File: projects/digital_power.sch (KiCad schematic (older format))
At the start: 5 parts, among them U501 LT1763

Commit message: updated LED indicators in schematic files (*.sch)
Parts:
- removed D?: LED_G, symbol LED
- added D?: GREEN_LED, symbol GREEN_LED
- added R?: 121, symbol R
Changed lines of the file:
@@
 LIBS:microchip_gosselin
 LIBS:linear_technology_gosselin
+LIBS:led_gosselin
 LIBS:mStereo2-cache
 EELAYER 24 0
@@
 	4450 4650 7000 4650
 $Comp
-L LED D?
-U 1 1 544F5650
-P 8100 4100
-F 0 "D?" H 8100 4200 50  0000 C CNN
-F 1 "LED_G" H 8100 4000 50  0000 C CNN
-F 2 "" H 8100 4100 60  0000 C CNN
-F 3 "" H 8100 4100 60  0000 C CNN
-	1    8100 4100
+L GREEN_LED D?
+U 1 1 5454AC46
+P 4000 4300
+F 0 "D?" H 4000 4400 50  0000 C CNN
+F 1 "GREEN_LED" H 4000 4200 50  0000 C CNN
+F 2 "" H 4000 4300 60  0000 C CNN
+F 3 "" H 4000 4300 60  0000 C CNN
+F 4 " 160-1423-1-ND" H 4200 4600 60  0001 C CNN "Supplier-PN"
+F 5 "Digi-key" H 4100 4500 60  0001 C CNN "Supplier"
+F 6 "LED GREEN CLEAR THIN 0805 SMD" H 4500 4900 60  0001 C CNN "Description"
+F 7 "Lite-On" H 4300 4700 60  0001 C CNN "Manu"
+F 8 "LTST-C171GKT" H 4400 4800 60  0001 C CNN "Manu-PN"
+	1    4000 4300
 	0    1    1    0
 $EndComp
+$Comp
+L R R?
+U 1 1 5454CACE
+P 3700 4300
+F 0 "R?" V 3780 4300 40  0000 C CNN
+F 1 "121" V 3707 4301 40  0000 C CNN
+F 2 "" V 3630 4300 30  0000 C CNN
+F 3 "" H 3700 4300 30  0000 C CNN
+F 4 "Digi-key" H 3700 4300 60  0001 C CNN "Supplier"
+F 5 "RNCP0805FTD121RCT-ND" H 3700 4300 60  0001 C CNN "Supplier-PN"
+F 6 "Stackpole" H 3700 4300 60  0001 C CNN "Manu"
+F 7 "RNCP0805FTD121R" H 3700 4300 60  0001 C CNN "Manu-PN"
+F 8 "RES 121 OHM 1/4W 1% 0805" H 3700 4300 60  0001 C CNN "Description"
+	1    3700 4300
+	1    0    0    -1
+$EndComp
 $EndSCHEMATC

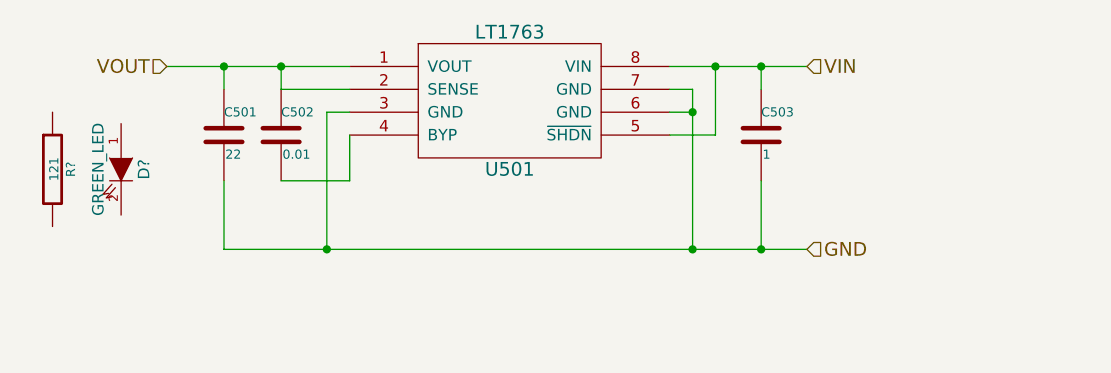
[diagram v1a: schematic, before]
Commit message: updated LEDs in schematic, output connectors, re-annotated
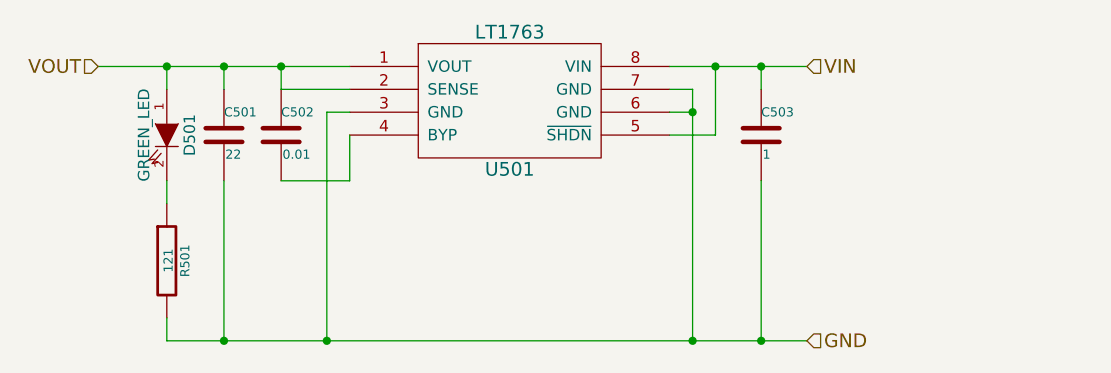
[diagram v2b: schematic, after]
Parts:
- removed C201: 22, symbol C
- removed C202: 0.01, symbol C
- removed C203: 1, symbol C
- added C501: 22, symbol C
- added C502: 0.01, symbol C
- added C503: 1, symbol C
- gave numbers to parts that had none: 2
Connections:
- net GND: now also R501.2, C501.2, C503.2
- net VIN: now also C503.1
- net VOUT: now also D501.1 (A), C501.1, C502.1
- net at U501.4 (BYP): now also C502.2
- net at D501.2 (K): now also R501.1
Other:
- moved on the sheet: D501, R501
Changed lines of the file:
@@
 Wire Wire Line
 	6500 4050 6400 4050
-Text HLabel 7000 4650 2    60   Input ~ 0
+Text HLabel 7000 5050 2    60   Input ~ 0
 GND
-Connection ~ 6500 4650
+Connection ~ 6500 5050
 $Comp
-L C C203
-U 1 1 54126F5E
+L C C503
+U 1 1 54571D8C
 P 6800 4150
-AR Path="/54126B8F/54126F5E" Ref="C203"  Part="1"
-AR Path="/541597AB/54126F5E" Ref="C503"  Part="1"
 F 0 "C503" H 6800 4250 40  0000 L CNN
 F 1 "1" H 6806 4065 40  0000 L CNN
@@
 $EndComp
 $Comp
-L C C201
-U 1 1 541271AA
+L C C501
+U 1 1 54571D8D
 P 4450 4150
-AR Path="/54126B8F/541271AA" Ref="C201"  Part="1"
-AR Path="/541597AB/541271AA" Ref="C501"  Part="1"
 F 0 "C501" H 4450 4250 40  0000 L CNN
 F 1 "22" H 4456 4065 40  0000 L CNN
@@
 $EndComp
 Connection ~ 6800 3850
-Connection ~ 6800 4650
-Text HLabel 4200 3850 0    60   Input ~ 0
+Connection ~ 6800 5050
+Text HLabel 3900 3850 0    60   Input ~ 0
 VOUT
 $Comp
-L C C202
-U 1 1 544A1569
+L C C502
+U 1 1 54571D8E
 P 4700 4150
-AR Path="/54126B8F/544A1569" Ref="C202"  Part="1"
-AR Path="/541597AB/544A1569" Ref="C502"  Part="1"
 F 0 "C502" H 4700 4250 40  0000 L CNN
 F 1 "0.01" H 4706 4065 40  0000 L CNN
@@
 $EndComp
 Wire Wire Line
-	4200 3850 5000 3850
+	3900 3850 4200 3850
 Wire Wire Line
-	6400 3850 7000 3850
+	4200 3850 4450 3850
+Wire Wire Line
+	4450 3850 4700 3850
+Wire Wire Line
+	4700 3850 5000 3850
+Wire Wire Line
+	6400 3850 6600 3850
+Wire Wire Line
+	6600 3850 6800 3850
+Wire Wire Line
+	6800 3850 7000 3850
 Wire Wire Line
 	6400 3950 6500 3950
 Wire Wire Line
-	6500 3950 6500 4650
+	6500 3950 6500 4050
+Wire Wire Line
+	6500 4050 6500 5050
 Connection ~ 6500 4050
 Wire Wire Line
 	6800 3850 6800 3950
 Wire Wire Line
-	6800 4650 6800 4350
+	6800 5050 6800 4350
 Wire Wire Line
 	6400 4150 6600 4150
@@
 	5000 4050 4900 4050
 Wire Wire Line
-	4900 4050 4900 4650
-Connection ~ 4900 4650
+	4900 4050 4900 5050
+Connection ~ 4900 5050
 Wire Wire Line
 	4700 3950 5000 3950
@@
 Connection ~ 4450 3850
 Wire Wire Line
-	4450 4350 4450 4650
+	4450 4350 4450 5050
 Wire Wire Line
-	4450 4650 7000 4650
+	4200 5050 4450 5050
+Wire Wire Line
+	4450 5050 4900 5050
+Wire Wire Line
+	4900 5050 6500 5050
+Wire Wire Line
+	6500 5050 6800 5050
+Wire Wire Line
+	6800 5050 7000 5050
 $Comp
-L GREEN_LED D?
+L GREEN_LED D501
 U 1 1 5454AC46
-P 4000 4300
-F 0 "D?" H 4000 4400 50  0000 C CNN
-F 1 "GREEN_LED" H 4000 4200 50  0000 C CNN
-F 2 "" H 4000 4300 60  0000 C CNN
-F 3 "" H 4000 4300 60  0000 C CNN
-F 4 " 160-1423-1-ND" H 4200 4600 60  0001 C CNN "Supplier-PN"
-F 5 "Digi-key" H 4100 4500 60  0001 C CNN "Supplier"
-F 6 "LED GREEN CLEAR THIN 0805 SMD" H 4500 4900 60  0001 C CNN "Description"
-F 7 "Lite-On" H 4300 4700 60  0001 C CNN "Manu"
-F 8 "LTST-C171GKT" H 4400 4800 60  0001 C CNN "Manu-PN"
-	1    4000 4300
+P 4200 4150
+F 0 "D501" H 4200 4250 50  0000 C CNN
+F 1 "GREEN_LED" H 4200 4050 50  0000 C CNN
+F 2 "" H 4200 4150 60  0000 C CNN
+F 3 "" H 4200 4150 60  0000 C CNN
+F 4 " 160-1423-1-ND" H 4400 4450 60  0001 C CNN "Supplier-PN"
+F 5 "Digi-key" H 4300 4350 60  0001 C CNN "Supplier"
+F 6 "LED GREEN CLEAR THIN 0805 SMD" H 4700 4750 60  0001 C CNN "Description"
+F 7 "Lite-On" H 4500 4550 60  0001 C CNN "Manu"
+F 8 "LTST-C171GKT" H 4600 4650 60  0001 C CNN "Manu-PN"
+	1    4200 4150
 	0    1    1    0
 $EndComp
 $Comp
-L R R?
+L R R501
 U 1 1 5454CACE
-P 3700 4300
-F 0 "R?" V 3780 4300 40  0000 C CNN
-F 1 "121" V 3707 4301 40  0000 C CNN
-F 2 "" V 3630 4300 30  0000 C CNN
-F 3 "" H 3700 4300 30  0000 C CNN
-F 4 "Digi-key" H 3700 4300 60  0001 C CNN "Supplier"
-F 5 "RNCP0805FTD121RCT-ND" H 3700 4300 60  0001 C CNN "Supplier-PN"
-F 6 "Stackpole" H 3700 4300 60  0001 C CNN "Manu"
-F 7 "RNCP0805FTD121R" H 3700 4300 60  0001 C CNN "Manu-PN"
-F 8 "RES 121 OHM 1/4W 1% 0805" H 3700 4300 60  0001 C CNN "Description"
-	1    3700 4300
+P 4200 4700
+F 0 "R501" V 4280 4700 40  0000 C CNN
+F 1 "121" V 4207 4701 40  0000 C CNN
+F 2 "" V 4130 4700 30  0000 C CNN
+F 3 "" H 4200 4700 30  0000 C CNN
+F 4 "Digi-key" H 4200 4700 60  0001 C CNN "Supplier"
+F 5 "RNCP0805FTD121RCT-ND" H 4200 4700 60  0001 C CNN "Supplier-PN"
+F 6 "Stackpole" H 4200 4700 60  0001 C CNN "Manu"
+F 7 "RNCP0805FTD121R" H 4200 4700 60  0001 C CNN "Manu-PN"
+F 8 "RES 121 OHM 1/4W 1% 0805" H 4200 4700 60  0001 C CNN "Description"
+	1    4200 4700
 	1    0    0    -1
 $EndComp
+Wire Wire Line
+	4200 3850 4200 3950
+Connection ~ 4200 3850
+Wire Wire Line
+	4200 4350 4200 4450
+Wire Wire Line
+	4200 5050 4200 4950
+Connection ~ 4450 5050
 $EndSCHEMATC

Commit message: updated power sheets
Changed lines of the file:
@@
 $EndComp
 Wire Wire Line
-	3900 3850 4200 3850
+	3900 3850 5000 3850
 Wire Wire Line
-	4200 3850 4450 3850
-Wire Wire Line
-	4450 3850 4700 3850
-Wire Wire Line
-	4700 3850 5000 3850
-Wire Wire Line
-	6400 3850 6600 3850
-Wire Wire Line
-	6600 3850 6800 3850
-Wire Wire Line
-	6800 3850 7000 3850
+	6400 3850 7000 3850
 Wire Wire Line
 	6400 3950 6500 3950
 Wire Wire Line
-	6500 3950 6500 4050
-Wire Wire Line
-	6500 4050 6500 5050
+	6500 5050 6500 3950
 Connection ~ 6500 4050
 Wire Wire Line
@@
 	5000 4050 4900 4050
 Wire Wire Line
-	4900 4050 4900 5050
+	4900 5050 4900 4050
 Connection ~ 4900 5050
 Wire Wire Line
@@
 	4450 4350 4450 5050
 Wire Wire Line
-	4200 5050 4450 5050
-Wire Wire Line
-	4450 5050 4900 5050
-Wire Wire Line
-	4900 5050 6500 5050
-Wire Wire Line
-	6500 5050 6800 5050
-Wire Wire Line
-	6800 5050 7000 5050
+	4200 5050 7000 5050
 $Comp
 L GREEN_LED D501

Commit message: updated cvpcb footprint/component links
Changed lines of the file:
@@
 	6400 3950 6500 3950
 Wire Wire Line
-	6500 5050 6500 3950
+	6500 3950 6500 5050
 Connection ~ 6500 4050
 Wire Wire Line
@@
 	5000 4050 4900 4050
 Wire Wire Line
-	4900 5050 4900 4050
+	4900 4050 4900 5050
 Connection ~ 4900 5050
 Wire Wire Line
